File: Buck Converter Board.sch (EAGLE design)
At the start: 7 parts, among them J1 POWERPOLE_POWER25A_HORIZONTAL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, J2 POWERPOLE_POWER25A_HORIZONTAL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

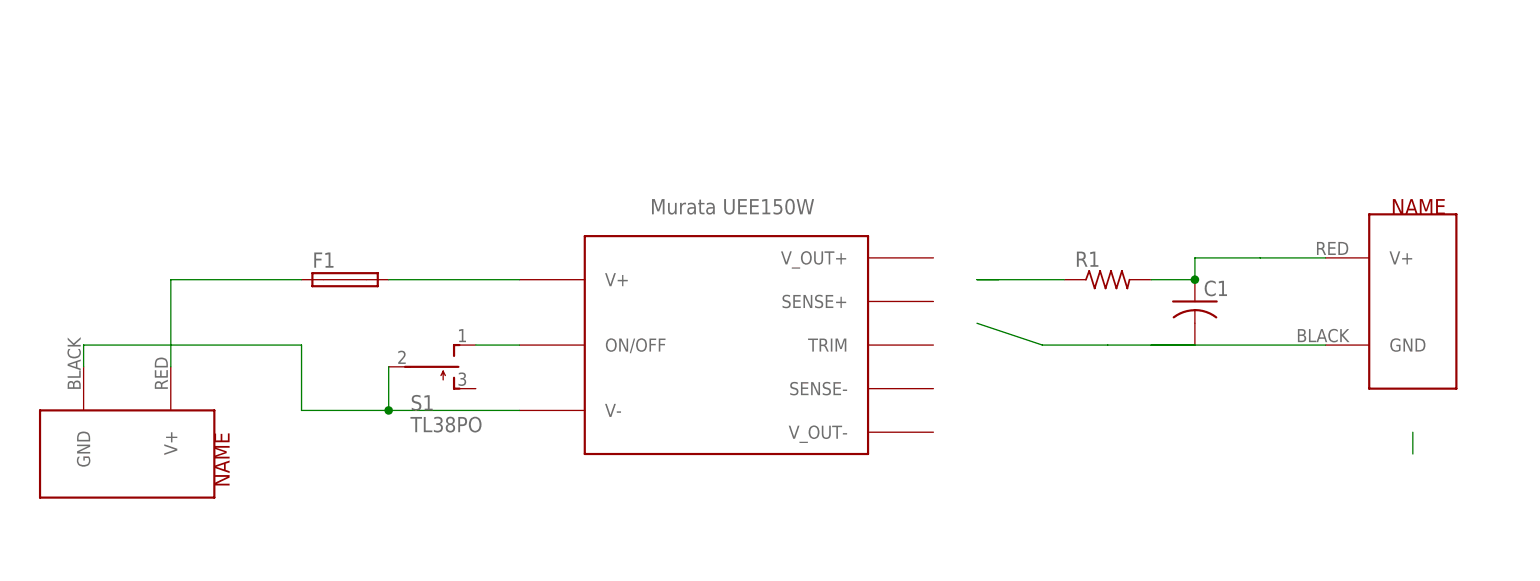
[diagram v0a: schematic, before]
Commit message: moved cmoponents on buck converter board around
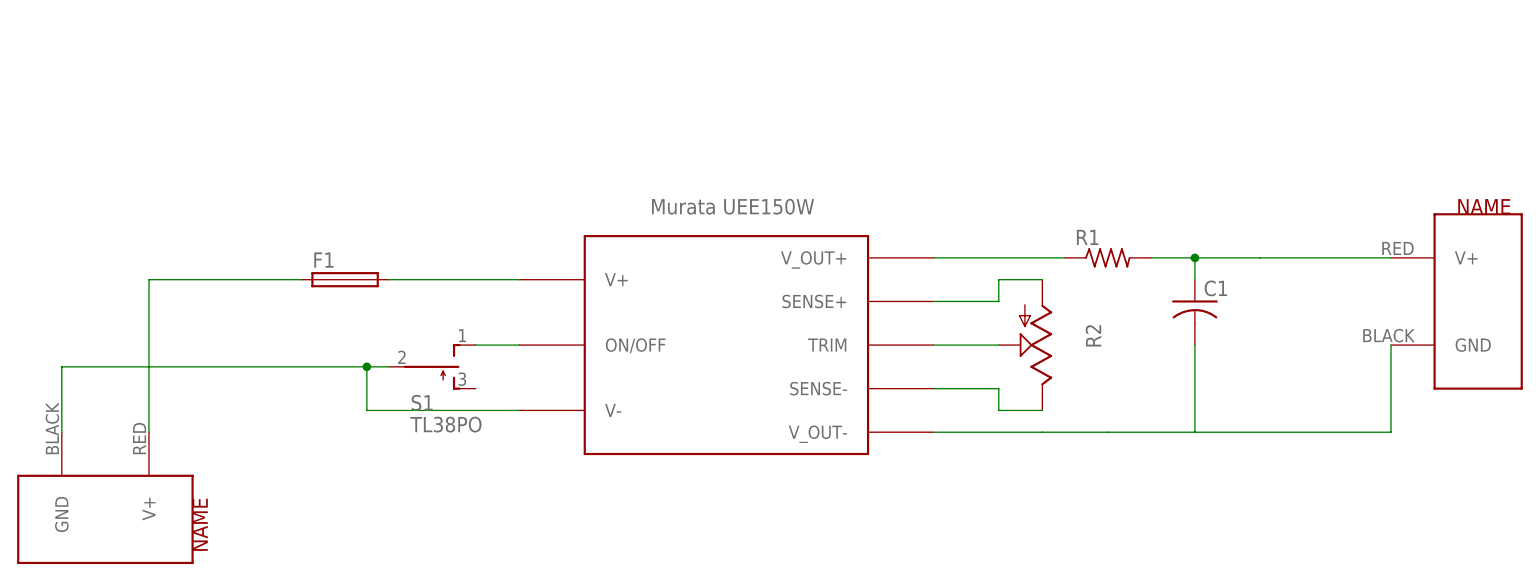
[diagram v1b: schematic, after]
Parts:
- added R2: (no value), pot:TRIM_US-B25P
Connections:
- new net N$10: R2.E, U$1.SENSE-
- new net N$7: R2.S, U$1.TRIM
- new net N$9: R2.A, U$1.SENSE+
- net N$4: now also U$1.V_OUT+
- net N$6: now also U$1.V_OUT-
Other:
- moved on the sheet: R1
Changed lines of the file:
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@@
 <part name="S1" library="switch" library_urn="urn:adsk.eagle:library:380" deviceset="TL38PO" device="" package3d_urn="urn:adsk.eagle:package:27745/1"/>
 <part name="U$1" library="REV Aux Circuit" deviceset="UEE150W" device=""/>
+<part name="R2" library="pot" library_urn="urn:adsk.eagle:library:331" deviceset="TRIM_US-" device="B25P" package3d_urn="urn:adsk.eagle:package:22684/1"/>
 </parts>
 <sheets>
@@
 <attribute name="NAME" x="29.21" y="64.897" size="1.778" layer="95"/>
 </instance>
-<instance part="R1" gate="G$1" x="121.92" y="63.5"/>
+<instance part="R1" gate="G$1" x="121.92" y="66.04"/>
 <instance part="C1" gate="G$1" x="132.08" y="60.96"/>
-<instance part="J1" gate="G$1" x="7.62" y="43.18" rot="R270"/>
-<instance part="J2" gate="G$1" x="157.48" y="60.96"/>
+<instance part="J1" gate="G$1" x="5.08" y="35.56" rot="R270"/>
+<instance part="J2" gate="G$1" x="165.1" y="60.96"/>
 <instance part="S1" gate="BEF1" x="43.18" y="53.34" rot="R270"/>
 <instance part="U$1" gate="G$1" x="60.96" y="43.18"/>
+<instance part="R2" gate="G$1" x="114.3" y="55.88" rot="R180"/>
 </instances>
 <busses>
@@
 <pinref part="J1" gate="G$1" pin="V+"/>
 <pinref part="F1" gate="G$1" pin="1"/>
-<wire x1="12.7" y1="53.34" x2="12.7" y2="63.5" width="0.1524" layer="91"/>
-<wire x1="12.7" y1="63.5" x2="27.94" y2="63.5" width="0.1524" layer="91"/>
+<wire x1="10.16" y1="45.72" x2="10.16" y2="63.5" width="0.1524" layer="91"/>
+<wire x1="10.16" y1="63.5" x2="27.94" y2="63.5" width="0.1524" layer="91"/>
 </segment>
 </net>
@@
 <segment>
 <pinref part="J1" gate="G$1" pin="GND"/>
-<wire x1="2.54" y1="53.34" x2="2.54" y2="55.88" width="0.1524" layer="91"/>
-<wire x1="2.54" y1="55.88" x2="27.94" y2="55.88" width="0.1524" layer="91"/>
-<wire x1="27.94" y1="55.88" x2="27.94" y2="48.26" width="0.1524" layer="91"/>
+<wire x1="0" y1="45.72" x2="0" y2="53.34" width="0.1524" layer="91"/>
+<wire x1="0" y1="53.34" x2="35.56" y2="53.34" width="0.1524" layer="91"/>
+<wire x1="35.56" y1="53.34" x2="35.56" y2="48.26" width="0.1524" layer="91"/>
 <pinref part="U$1" gate="G$1" pin="V-"/>
-<wire x1="27.94" y1="48.26" x2="38.1" y2="48.26" width="0.1524" layer="91"/>
+<wire x1="35.56" y1="48.26" x2="53.34" y2="48.26" width="0.1524" layer="91"/>
 <pinref part="S1" gate="BEF1" pin="P"/>
-<wire x1="38.1" y1="48.26" x2="53.34" y2="48.26" width="0.1524" layer="91"/>
-<wire x1="38.1" y1="48.26" x2="38.1" y2="53.34" width="0.1524" layer="91"/>
-<junction x="38.1" y="48.26"/>
-</segment>
-</net>
-<net name="N$4" class="0">
-<segment>
-<pinref part="R1" gate="G$1" pin="1"/>
-<wire x1="109.22" y1="63.5" x2="106.68" y2="63.5" width="0.1524" layer="91"/>
-<wire x1="106.68" y1="63.5" x2="116.84" y2="63.5" width="0.1524" layer="91"/>
+<wire x1="35.56" y1="53.34" x2="38.1" y2="53.34" width="0.1524" layer="91"/>
+<junction x="35.56" y="53.34"/>
 </segment>
 </net>
 <net name="N$5" class="0">
 <segment>
-<pinref part="R1" gate="G$1" pin="2"/>
 <pinref part="C1" gate="G$1" pin="1"/>
-<wire x1="127" y1="63.5" x2="132.08" y2="63.5" width="0.1524" layer="91"/>
 <pinref part="J2" gate="G$1" pin="V+"/>
 <wire x1="132.08" y1="63.5" x2="132.08" y2="66.04" width="0.1524" layer="91"/>
 <wire x1="132.08" y1="66.04" x2="139.7" y2="66.04" width="0.1524" layer="91"/>
-<junction x="132.08" y="63.5"/>
-<wire x1="139.7" y1="66.04" x2="147.32" y2="66.04" width="0.1524" layer="91"/>
+<junction x="132.08" y="66.04"/>
+<wire x1="139.7" y1="66.04" x2="154.94" y2="66.04" width="0.1524" layer="91"/>
+<pinref part="R1" gate="G$1" pin="2"/>
+<wire x1="132.08" y1="66.04" x2="127" y2="66.04" width="0.1524" layer="91"/>
 </segment>
 </net>
@@
 <segment>
 <pinref part="C1" gate="G$1" pin="2"/>
-<wire x1="132.08" y1="55.88" x2="127" y2="55.88" width="0.1524" layer="91"/>
-<wire x1="127" y1="55.88" x2="121.92" y2="55.88" width="0.1524" layer="91"/>
-<wire x1="121.92" y1="55.88" x2="114.3" y2="55.88" width="0.1524" layer="91"/>
-<wire x1="114.3" y1="55.88" x2="106.68" y2="58.42" width="0.1524" layer="91"/>
+<wire x1="132.08" y1="55.88" x2="132.08" y2="45.72" width="0.1524" layer="91"/>
+<wire x1="132.08" y1="45.72" x2="121.92" y2="45.72" width="0.1524" layer="91"/>
+<wire x1="121.92" y1="45.72" x2="114.3" y2="45.72" width="0.1524" layer="91"/>
 <pinref part="J2" gate="G$1" pin="GND"/>
-<wire x1="147.32" y1="55.88" x2="127" y2="55.88" width="0.1524" layer="91"/>
-</segment>
-</net>
-<net name="N$7" class="0">
-<segment>
-<wire x1="157.48" y1="43.18" x2="157.48" y2="45.72" width="0.1524" layer="91"/>
+<wire x1="154.94" y1="55.88" x2="154.94" y2="45.72" width="0.1524" layer="91"/>
+<wire x1="154.94" y1="45.72" x2="132.08" y2="45.72" width="0.1524" layer="91"/>
+<pinref part="U$1" gate="G$1" pin="V_OUT-"/>
+<wire x1="101.6" y1="45.72" x2="114.3" y2="45.72" width="0.1524" layer="91"/>
 </segment>
 </net>
@@
 </segment>
 </net>
+<net name="N$4" class="0">
+<segment>
+<pinref part="R1" gate="G$1" pin="1"/>
+<pinref part="U$1" gate="G$1" pin="V_OUT+"/>
+<wire x1="116.84" y1="66.04" x2="101.6" y2="66.04" width="0.1524" layer="91"/>
+</segment>
+</net>
+<net name="N$7" class="0">
+<segment>
+<pinref part="U$1" gate="G$1" pin="TRIM"/>
+<pinref part="R2" gate="G$1" pin="S"/>
+<wire x1="101.6" y1="55.88" x2="109.22" y2="55.88" width="0.1524" layer="91"/>
+</segment>
+</net>
+<net name="N$9" class="0">
+<segment>
+<pinref part="U$1" gate="G$1" pin="SENSE+"/>
+<wire x1="101.6" y1="60.96" x2="109.22" y2="60.96" width="0.1524" layer="91"/>
+<wire x1="109.22" y1="60.96" x2="109.22" y2="63.5" width="0.1524" layer="91"/>
+<pinref part="R2" gate="G$1" pin="A"/>
+<wire x1="109.22" y1="63.5" x2="114.3" y2="63.5" width="0.1524" layer="91"/>
+</segment>
+</net>
+<net name="N$10" class="0">
+<segment>
+<pinref part="R2" gate="G$1" pin="E"/>
+<wire x1="114.3" y1="48.26" x2="109.22" y2="48.26" width="0.1524" layer="91"/>
+<wire x1="109.22" y1="48.26" x2="109.22" y2="50.8" width="0.1524" layer="91"/>
+<pinref part="U$1" gate="G$1" pin="SENSE-"/>
+<wire x1="109.22" y1="50.8" x2="101.6" y2="50.8" width="0.1524" layer="91"/>
+</segment>
+</net>

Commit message: removed trim pot and bullshit from buck board
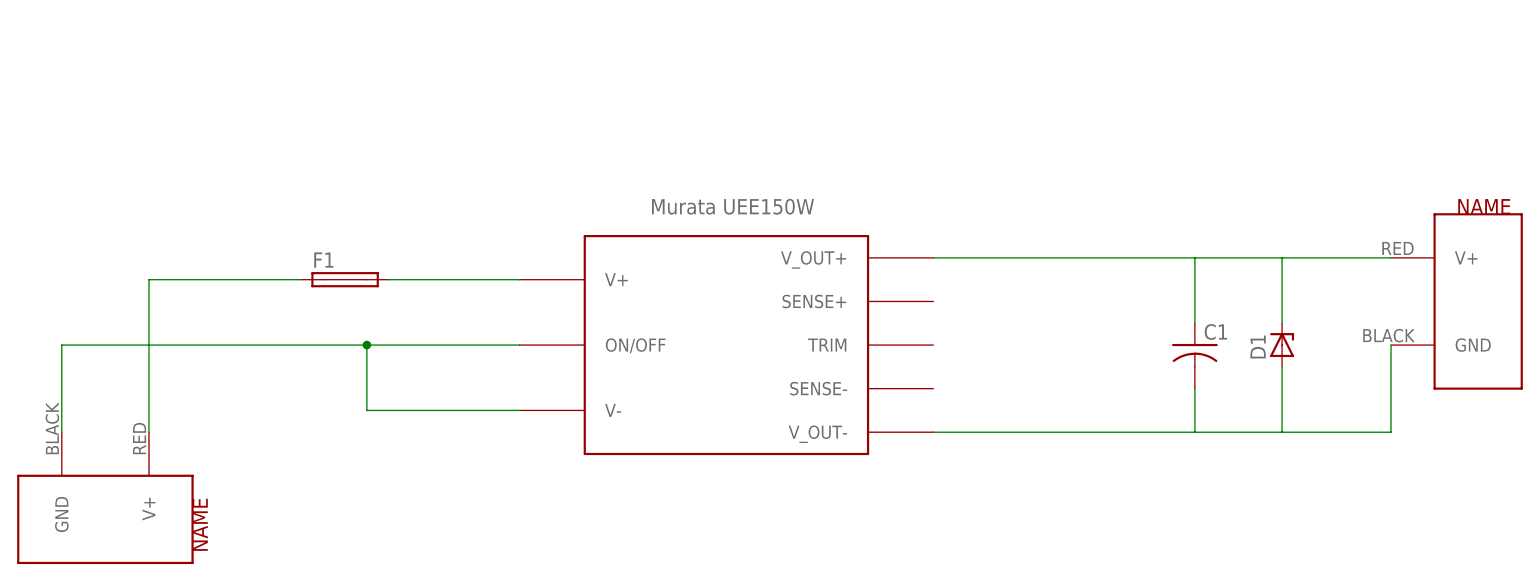
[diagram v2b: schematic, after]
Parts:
- removed R1: (no value), rcl:R-US_R0805
- removed R2: (no value), pot:TRIM_US-B25P
- removed S1: TL38PO, switch:TL38PO
- added D1: (no value), diode:ZENER-DIODESMB
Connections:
- removed net N$10: R2.E, U$1.SENSE-
- removed net N$7: R2.S, U$1.TRIM
- removed net N$8: S1.O, U$1.ON/OFF
- removed net N$9: R2.A, U$1.SENSE+
- new net N$11: D1.C
- new net N$12: D1.A
- net N$3: now also U$1.ON/OFF; no longer S1.P
- net N$4: now also J2.V+; no longer R1.1
- net N$5: no longer J2.V+, R1.2
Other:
- moved on the sheet: C1
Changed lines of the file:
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@@
 <layer number="97" name="Info" color="7" fill="1" visible="yes" active="yes"/>
 <layer number="98" name="Guide" color="6" fill="1" visible="yes" active="yes"/>
+<layer number="99" name="SpiceOrder" color="5" fill="1" visible="yes" active="yes"/>
 </layers>
 <schematic xreflabel="%F%N/%S.%C%R" xrefpart="/%S.%C%R">
@@
 <parts>
 <part name="F1" library="fuse" library_urn="urn:adsk.eagle:library:233" deviceset="FUSE" device="BLANK_5X20MM" package3d_urn="urn:adsk.eagle:package:14079/1"/>
-<part name="R1" library="rcl" library_urn="urn:adsk.eagle:library:334" deviceset="R-US_" device="R0805" package3d_urn="urn:adsk.eagle:package:23553/2"/>
 <part name="C1" library="rcl" library_urn="urn:adsk.eagle:library:334" deviceset="C-US" device="C0805" package3d_urn="urn:adsk.eagle:package:23617/2"/>
 <part name="J1" library="powerpoles" deviceset="POWERPOLE_POWER" device="25A_HORIZONTAL_G2"/>
 <part name="J2" library="powerpoles" deviceset="POWERPOLE_POWER" device="25A_HORIZONTAL_G2"/>
-<part name="S1" library="switch" library_urn="urn:adsk.eagle:library:380" deviceset="TL38PO" device="" package3d_urn="urn:adsk.eagle:package:27745/1"/>
 <part name="U$1" library="REV Aux Circuit" deviceset="UEE150W" device=""/>
-<part name="R2" library="pot" library_urn="urn:adsk.eagle:library:331" deviceset="TRIM_US-" device="B25P" package3d_urn="urn:adsk.eagle:package:22684/1"/>
+<part name="D1" library="diode" library_urn="urn:adsk.eagle:library:210" deviceset="ZENER-DIODE" device="SMB" package3d_urn="urn:adsk.eagle:package:43404/2"/>
 </parts>
 <sheets>
@@
 <attribute name="NAME" x="29.21" y="64.897" size="1.778" layer="95"/>
 </instance>
-<instance part="R1" gate="G$1" x="121.92" y="66.04"/>
-<instance part="C1" gate="G$1" x="132.08" y="60.96"/>
+<instance part="C1" gate="G$1" x="132.08" y="55.88"/>
 <instance part="J1" gate="G$1" x="5.08" y="35.56" rot="R270"/>
 <instance part="J2" gate="G$1" x="165.1" y="60.96"/>
-<instance part="S1" gate="BEF1" x="43.18" y="53.34" rot="R270"/>
 <instance part="U$1" gate="G$1" x="60.96" y="43.18"/>
-<instance part="R2" gate="G$1" x="114.3" y="55.88" rot="R180"/>
+<instance part="D1" gate="G$1" x="142.24" y="55.88" rot="R90"/>
 </instances>
 <busses>
@@
 <segment>
 <pinref part="J1" gate="G$1" pin="GND"/>
-<wire x1="0" y1="45.72" x2="0" y2="53.34" width="0.1524" layer="91"/>
-<wire x1="0" y1="53.34" x2="35.56" y2="53.34" width="0.1524" layer="91"/>
-<wire x1="35.56" y1="53.34" x2="35.56" y2="48.26" width="0.1524" layer="91"/>
+<wire x1="0" y1="45.72" x2="0" y2="55.88" width="0.1524" layer="91"/>
+<wire x1="0" y1="55.88" x2="35.56" y2="55.88" width="0.1524" layer="91"/>
+<wire x1="35.56" y1="55.88" x2="35.56" y2="48.26" width="0.1524" layer="91"/>
 <pinref part="U$1" gate="G$1" pin="V-"/>
 <wire x1="35.56" y1="48.26" x2="53.34" y2="48.26" width="0.1524" layer="91"/>
-<pinref part="S1" gate="BEF1" pin="P"/>
-<wire x1="35.56" y1="53.34" x2="38.1" y2="53.34" width="0.1524" layer="91"/>
-<junction x="35.56" y="53.34"/>
+<junction x="35.56" y="55.88"/>
+<pinref part="U$1" gate="G$1" pin="ON/OFF"/>
+<wire x1="35.56" y1="55.88" x2="53.34" y2="55.88" width="0.1524" layer="91"/>
+</segment>
+</net>
+<net name="N$6" class="0">
+<segment>
+<pinref part="C1" gate="G$1" pin="2"/>
+<wire x1="132.08" y1="50.8" x2="132.08" y2="45.72" width="0.1524" layer="91"/>
+<pinref part="J2" gate="G$1" pin="GND"/>
+<wire x1="154.94" y1="55.88" x2="154.94" y2="45.72" width="0.1524" layer="91"/>
+<wire x1="154.94" y1="45.72" x2="132.08" y2="45.72" width="0.1524" layer="91"/>
+<pinref part="U$1" gate="G$1" pin="V_OUT-"/>
+<wire x1="101.6" y1="45.72" x2="132.08" y2="45.72" width="0.1524" layer="91"/>
+</segment>
+</net>
+<net name="N$4" class="0">
+<segment>
+<pinref part="U$1" gate="G$1" pin="V_OUT+"/>
+<wire x1="154.94" y1="66.04" x2="101.6" y2="66.04" width="0.1524" layer="91"/>
+<pinref part="J2" gate="G$1" pin="V+"/>
 </segment>
 </net>
@@
 <segment>
 <pinref part="C1" gate="G$1" pin="1"/>
-<pinref part="J2" gate="G$1" pin="V+"/>
-<wire x1="132.08" y1="63.5" x2="132.08" y2="66.04" width="0.1524" layer="91"/>
-<wire x1="132.08" y1="66.04" x2="139.7" y2="66.04" width="0.1524" layer="91"/>
-<junction x="132.08" y="66.04"/>
-<wire x1="139.7" y1="66.04" x2="154.94" y2="66.04" width="0.1524" layer="91"/>
-<pinref part="R1" gate="G$1" pin="2"/>
-<wire x1="132.08" y1="66.04" x2="127" y2="66.04" width="0.1524" layer="91"/>
+<wire x1="132.08" y1="58.42" x2="132.08" y2="66.04" width="0.1524" layer="91"/>
 </segment>
 </net>
-<net name="N$6" class="0">
+<net name="N$11" class="0">
 <segment>
-<pinref part="C1" gate="G$1" pin="2"/>
-<wire x1="132.08" y1="55.88" x2="132.08" y2="45.72" width="0.1524" layer="91"/>
-<wire x1="132.08" y1="45.72" x2="121.92" y2="45.72" width="0.1524" layer="91"/>
-<wire x1="121.92" y1="45.72" x2="114.3" y2="45.72" width="0.1524" layer="91"/>
-<pinref part="J2" gate="G$1" pin="GND"/>
-<wire x1="154.94" y1="55.88" x2="154.94" y2="45.72" width="0.1524" layer="91"/>
-<wire x1="154.94" y1="45.72" x2="132.08" y2="45.72" width="0.1524" layer="91"/>
-<pinref part="U$1" gate="G$1" pin="V_OUT-"/>
-<wire x1="101.6" y1="45.72" x2="114.3" y2="45.72" width="0.1524" layer="91"/>
+<pinref part="D1" gate="G$1" pin="C"/>
+<wire x1="142.24" y1="58.42" x2="142.24" y2="66.04" width="0.1524" layer="91"/>
 </segment>
 </net>
-<net name="N$8" class="0">
+<net name="N$12" class="0">
 <segment>
-<pinref part="S1" gate="BEF1" pin="O"/>
-<wire x1="48.26" y1="55.88" x2="53.34" y2="55.88" width="0.1524" layer="91"/>
-<pinref part="U$1" gate="G$1" pin="ON/OFF"/>
+<pinref part="D1" gate="G$1" pin="A"/>
+<wire x1="142.24" y1="45.72" x2="142.24" y2="53.34" width="0.1524" layer="91"/>
 </segment>
 </net>
-<net name="N$4" class="0">
-<segment>
-<pinref part="R1" gate="G$1" pin="1"/>
-<pinref part="U$1" gate="G$1" pin="V_OUT+"/>
-<wire x1="116.84" y1="66.04" x2="101.6" y2="66.04" width="0.1524" layer="91"/>
-</segment>
-</net>
-<net name="N$7" class="0">
-<segment>
-<pinref part="U$1" gate="G$1" pin="TRIM"/>
-<pinref part="R2" gate="G$1" pin="S"/>
-<wire x1="101.6" y1="55.88" x2="109.22" y2="55.88" width="0.1524" layer="91"/>
-</segment>
-</net>
-<net name="N$9" class="0">
-<segment>
-<pinref part="U$1" gate="G$1" pin="SENSE+"/>
-<wire x1="101.6" y1="60.96" x2="109.22" y2="60.96" width="0.1524" layer="91"/>
-<wire x1="109.22" y1="60.96" x2="109.22" y2="63.5" width="0.1524" layer="91"/>
-<pinref part="R2" gate="G$1" pin="A"/>
-<wire x1="109.22" y1="63.5" x2="114.3" y2="63.5" width="0.1524" layer="91"/>
-</segment>
-</net>
-<net name="N$10" class="0">
-<segment>
-<pinref part="R2" gate="G$1" pin="E"/>
-<wire x1="114.3" y1="48.26" x2="109.22" y2="48.26" width="0.1524" layer="91"/>
-<wire x1="109.22" y1="48.26" x2="109.22" y2="50.8" width="0.1524" layer="91"/>
-<pinref part="U$1" gate="G$1" pin="SENSE-"/>
-<wire x1="109.22" y1="50.8" x2="101.6" y2="50.8" width="0.1524" layer="91"/>
-</segment>
-</net>
